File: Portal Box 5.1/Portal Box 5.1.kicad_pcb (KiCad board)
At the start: 2 copper layers, 120 x 80 mm, 79 parts, among them J1 609-87520-0010ALFCT-ND, J2 2073-USB4105-GF-ACT-ND, J3 A 14-LC-TT, J4 732-6001-1-ND, J5 RFID-RC522, J6 Conn_01x04, K1 PR28-5V-360-1A-E, Q1 NTR5103NT1G, Q2 NTR5103NT1G, SW1 141-TL3336AF160QCT-ND, SW2 SW_DPST, U1 497-5026-1-ND, U2 497-5026-1-ND, U3 448-TLE4971A050T5UE0001XUMA1C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, U4 AP7363-33D-13, U5 ESP32-S3-DEVKITC-1-N8R8-OFFIC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

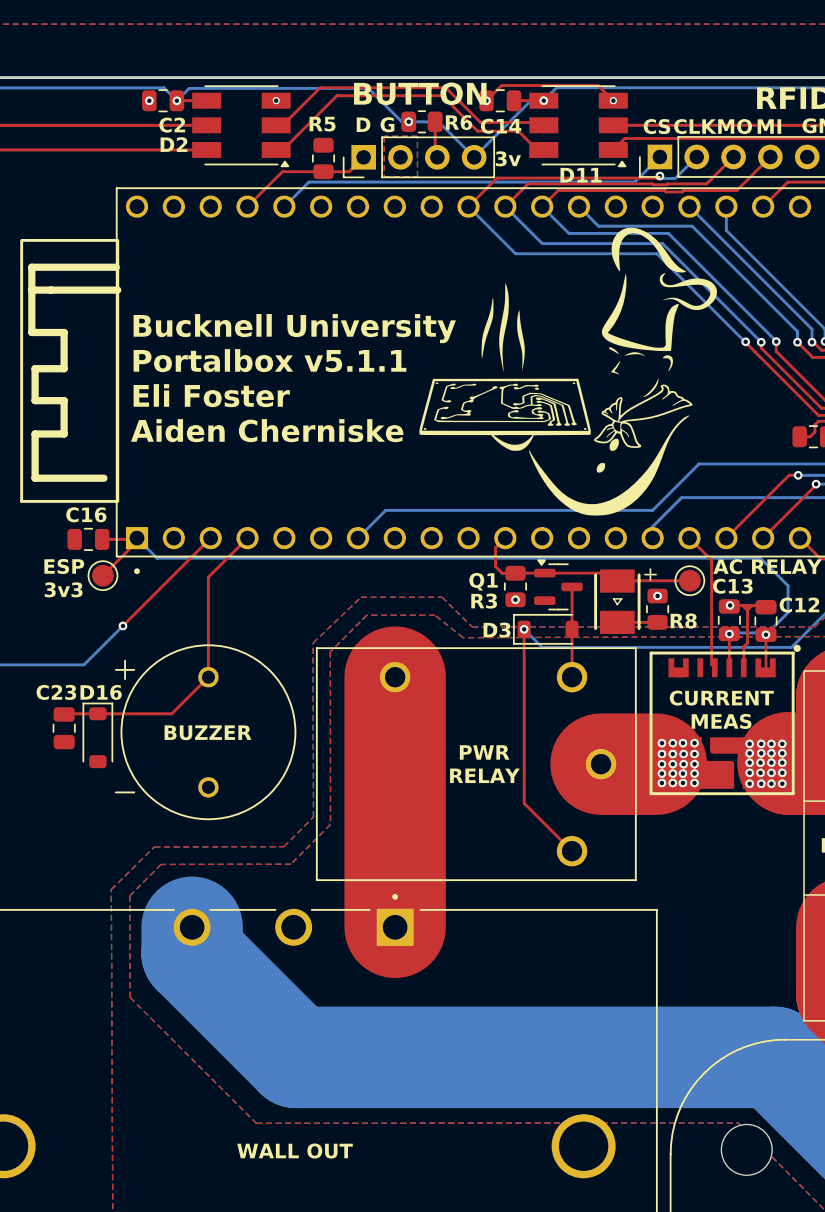
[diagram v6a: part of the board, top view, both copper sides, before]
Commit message: schematic updates, added ground jumper
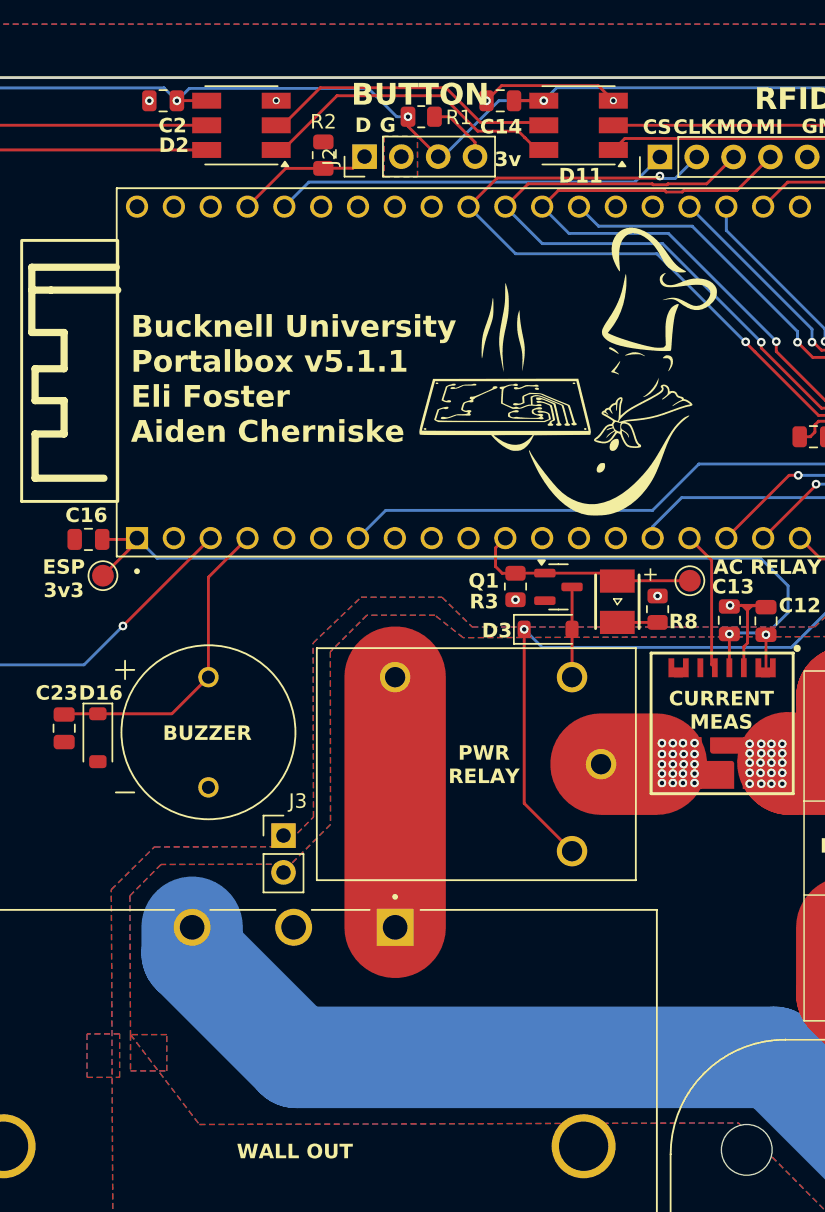
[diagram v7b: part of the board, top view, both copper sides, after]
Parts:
- removed the R5 at (123.1, 58.7)
- removed the R6 at (129.9, 56.2)
- removed SW2: SW_DPST, Connector_PinHeader_2.54mm:PinHeader_1x04_P2.54mm_Vertical
- added J2: Conn_01x04, Connector_PinHeader_2.54mm:PinHeader_1x04_P2.54mm_Vertical, F.Cu at (125.9, 58.6)
- added J3: Conn_01x02, Connector_PinHeader_2.54mm:PinHeader_1x02_P2.54mm_Vertical, F.Cu at (120.3, 105.4)
- added R1: 1k, Resistor_SMD:R_0805_2012Metric, F.Cu at (129.8, 55.9)
- added R2: 10k, Resistor_SMD:R_0805_2012Metric, F.Cu at (123.1, 58.5)
- renumbered C19 to C1, C18 to C10, C17 to C11, C20 to C12, C21 to C13, C1 to C14, C5 to C15, C7 to C16, C10 to C17, C14 to C18, C2 to C19, C23 to C2, C6 to C20, C8 to C21, C11 to C22, C15 to C23, C12 to C3, C13 to C4, C22 to C5, C9 to C6, C16 to C7, C3 to C8, C4 to C9, D16 to D1, D9 to D10, D2 to D12, D5 to D13, D8 to D14, D10 to D15, D12 to D16, D13 to D2, D14 to D4, D15 to D5, D1 to D7, D4 to D8, D7 to D9, J6 to J1, J1 to J6, J2 to J7, J3 to J8, R1 to R10, R2 to R11, R10 to R3, R7 to R4, R11 to R5, R8 to R6, R3 to R7, R9 to R8, R4 to R9, TP3 to TP2, TP2 to TP3, U3 to U1, U1 to U2, U5 to U3, U2 to U4, U4 to U5
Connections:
- net /CO9 renamed /CO11
- net /DO9 renamed /DO11
- D16 pad 5: /CO10 -> unconnected-(D16-CO-Pad5)
- D16 pad 6: /DO10 -> unconnected-(D16-DO-Pad6)
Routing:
- net Net-(J2-Pin_4): track 0.00 -> 4.52 mm
- net /LED_3V: track 2.51 -> 0.00 mm
- net BUTTON: track 9.42 -> 9.50 mm, vias 0 -> 1
- net GND: vias 60 -> 59
- added copper zone on B.Cu, net BUTTON
- added copper zone on F.Cu, net BUTTON
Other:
- board text removed: "R5"
- board text removed: "R6"

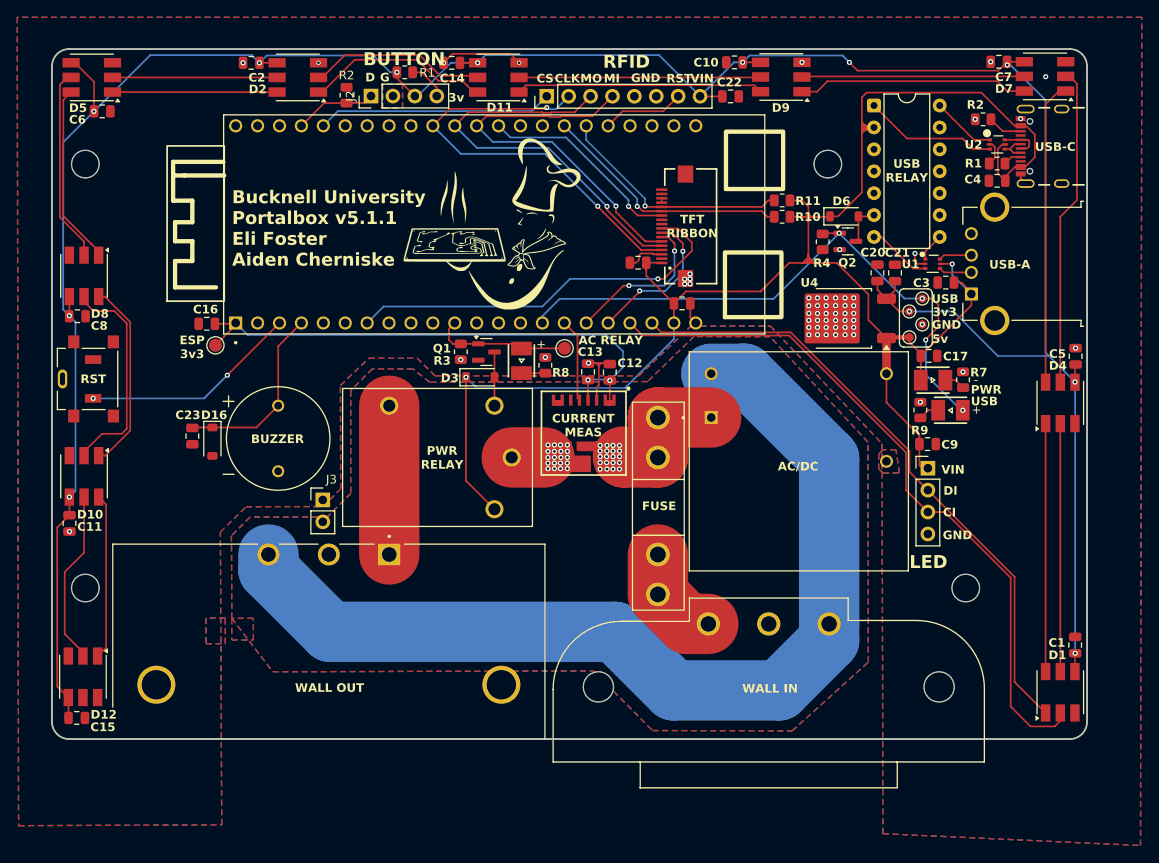
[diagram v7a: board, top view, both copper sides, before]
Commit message: update component labels
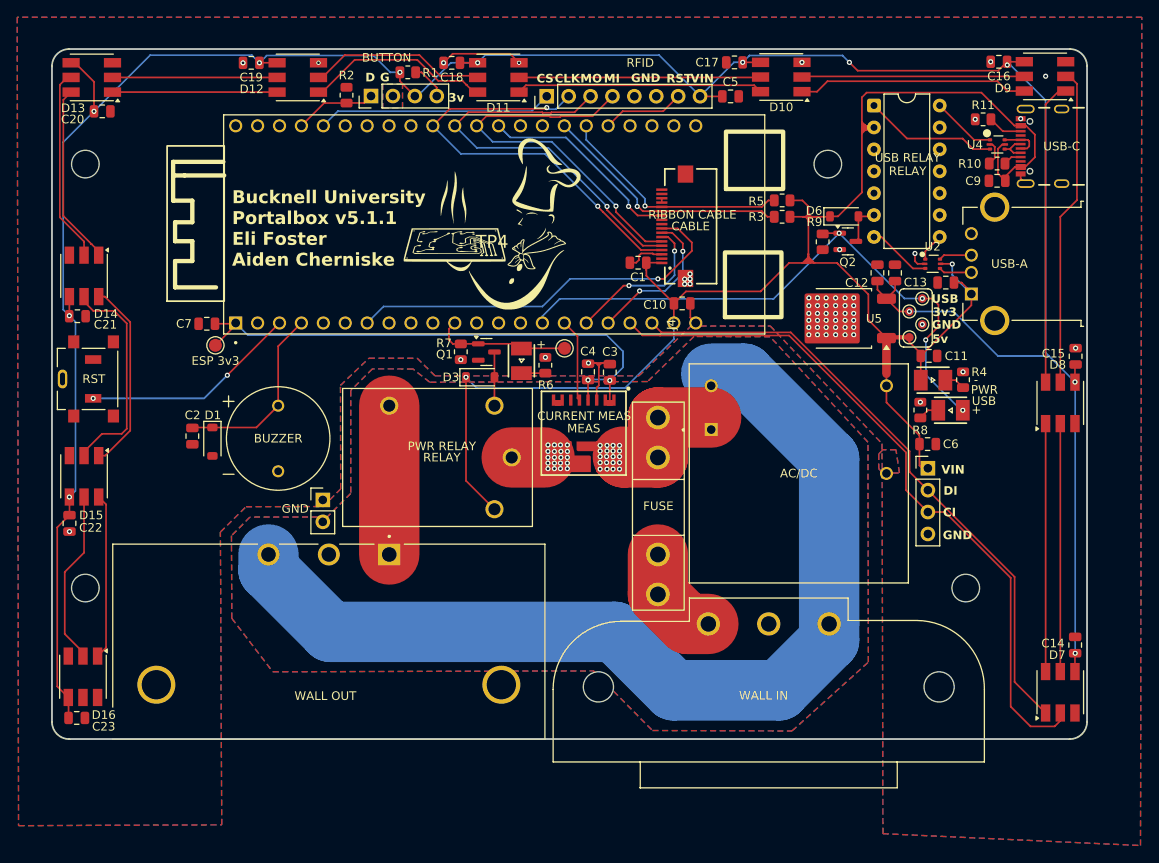
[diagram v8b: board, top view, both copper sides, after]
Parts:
- moved PS1 1.40 mm to (175.5, 102.3)
- moved R1 0.35 mm to (130.2, 55.9)
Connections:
- J4 pad 10: SD_CS -> unconnected-(J4-Pad10)
- J4 pad 11: MEM_CS -> unconnected-(J4-Pad11)
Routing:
- net GND: vias 59 -> 60
- net BUTTON: vias 1 -> 0
- removed copper zone on B.Cu, net BUTTON
- removed copper zone on F.Cu, net BUTTON
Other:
- board text removed: "AC RELAY"
- board text removed: "AC/DC"
- board text removed: "BUTTON"
- board text removed: "C1"
- board text removed: "C10"
- board text removed: "C11"
- board text removed: "C12"
- board text removed: "C13"
- board text removed: "C14"
- board text removed: "C15"
- board text removed: "C16"
- board text removed: "C17"
- board text removed: "C2"
- board text removed: "C20"
- board text removed: "C21"
- board text removed: "C22"
- board text removed: "C23"
- board text removed: "C3"
- board text removed: "C4"
- board text removed: "C5"
- board text removed: "C6"
- board text removed: "C7"
- board text removed: "C8"
- board text removed: "C9"
- board text removed: "CURRENT MEAS"
- board text removed: "D1"
- board text removed: "D10"
- board text removed: "D11"
- board text removed: "D12"
- board text removed: "D16"
- board text removed: "D2"
- board text removed: "D3"
- board text removed: "D4"
- board text removed: "D5"
- board text removed: "D6"
- board text removed: "D7"
- board text removed: "D8"
- board text removed: "D9"
- board text removed: "ESP 3v3"
- board text removed: "FUSE"
- board text removed: "LED"
- board text removed: "PWR"
- board text removed: "PWR RELAY"
- board text removed: "Q1"
- board text removed: "Q2"
- board text removed: "R1"
- board text removed: "R10"
- board text removed: "R11"
- board text removed: "R2"
- board text removed: "R3"
- board text removed: "R4"
- board text removed: "R7"
- board text removed: "R8"
- board text removed: "R9"
- board text removed: "RFID"
- board text removed: "TFT RIBBON"
- board text removed: "U1"
- board text removed: "U2"
- board text removed: "U4"
- board text removed: "USB RELAY"
- board text removed: "USB-A"
- board text removed: "USB-C"
- board text removed: "WALL IN"
- board text removed: "WALL OUT"
